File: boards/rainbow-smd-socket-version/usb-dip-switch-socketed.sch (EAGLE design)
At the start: 19 parts, among them SW1 KMR211NGLFS, SW2 110-47-316-41-105000, U1 PIC16F1459-I/SS, U2 PRTR5V0U2X

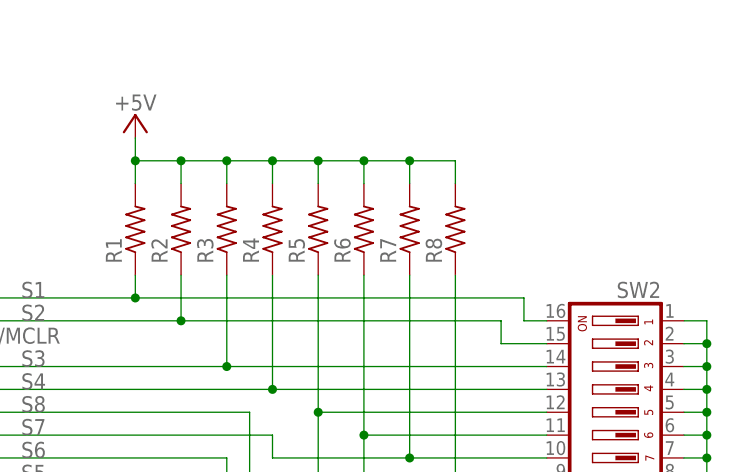
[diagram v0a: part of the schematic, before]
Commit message: add 100k value for pullup resistors R1-R8
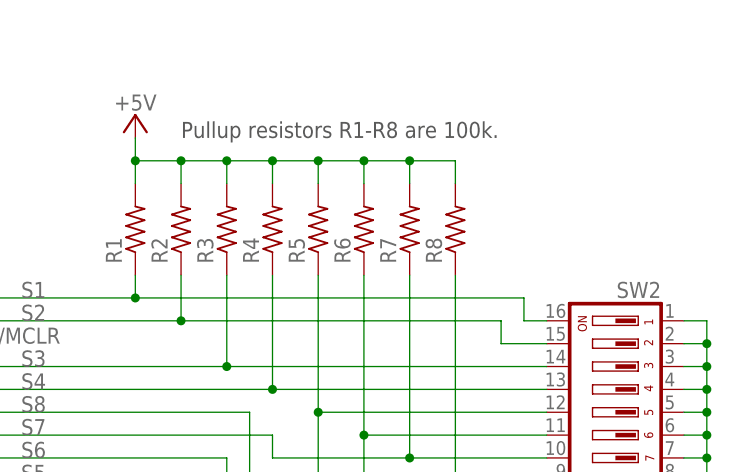
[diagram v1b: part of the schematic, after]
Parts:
- R1, R2, R3, R4, R5, R6, R7, R8: value (none) -> 100k
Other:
- note added: "Pullup resistors R1-R8 are 100k."
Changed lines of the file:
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@@
 <part name="SW2" library="Glen-MillMax-110-47-316-41-105000" deviceset="110-47-316-41-105000" device=""/>
 <part name="SUPPLY7" library="supply2" deviceset="GND" device=""/>
-<part name="R1" library="rcl" deviceset="R-US_" device="R0603"/>
-<part name="R2" library="rcl" deviceset="R-US_" device="R0603"/>
-<part name="R3" library="rcl" deviceset="R-US_" device="R0603"/>
-<part name="R4" library="rcl" deviceset="R-US_" device="R0603"/>
-<part name="R5" library="rcl" deviceset="R-US_" device="R0603"/>
-<part name="R6" library="rcl" deviceset="R-US_" device="R0603"/>
-<part name="R7" library="rcl" deviceset="R-US_" device="R0603"/>
-<part name="R8" library="rcl" deviceset="R-US_" device="R0603"/>
+<part name="R1" library="rcl" deviceset="R-US_" device="R0603" value="100k"/>
+<part name="R2" library="rcl" deviceset="R-US_" device="R0603" value="100k"/>
+<part name="R3" library="rcl" deviceset="R-US_" device="R0603" value="100k"/>
+<part name="R4" library="rcl" deviceset="R-US_" device="R0603" value="100k"/>
+<part name="R5" library="rcl" deviceset="R-US_" device="R0603" value="100k"/>
+<part name="R6" library="rcl" deviceset="R-US_" device="R0603" value="100k"/>
+<part name="R7" library="rcl" deviceset="R-US_" device="R0603" value="100k"/>
+<part name="R8" library="rcl" deviceset="R-US_" device="R0603" value="100k"/>
 <part name="P+4" library="supply1" deviceset="+5V" device=""/>
 </parts>
@@
 <text x="165.1" y="86.36" size="3.81" layer="97">ESD Protection</text>
 <text x="215.9" y="114.3" size="1.778" layer="97" align="top-left">ERG SDS-8-014</text>
+<text x="177.8" y="162.56" size="1.778" layer="97">Pullup resistors R1-R8 are 100k.</text>
 </plain>
 <instances>
@@
 <instance part="SW2" gate="G$1" x="226.06" y="137.16" rot="MR270"/>
 <instance part="SUPPLY7" gate="GND" x="236.22" y="119.38" rot="MR0"/>
-<instance part="R1" gate="G$1" x="172.72" y="152.4" rot="R90"/>
-<instance part="R2" gate="G$1" x="177.8" y="152.4" rot="R90"/>
-<instance part="R3" gate="G$1" x="182.88" y="152.4" rot="R90"/>
-<instance part="R4" gate="G$1" x="187.96" y="152.4" rot="R90"/>
-<instance part="R5" gate="G$1" x="193.04" y="152.4" rot="R90"/>
-<instance part="R6" gate="G$1" x="198.12" y="152.4" rot="R90"/>
-<instance part="R7" gate="G$1" x="203.2" y="152.4" rot="R90"/>
-<instance part="R8" gate="G$1" x="208.28" y="152.4" rot="R90"/>
+<instance part="R1" gate="G$1" x="172.72" y="152.4" smashed="yes" rot="R90">
+<attribute name="NAME" x="171.2214" y="148.59" size="1.778" layer="95" rot="R90"/>
+</instance>
+<instance part="R2" gate="G$1" x="177.8" y="152.4" smashed="yes" rot="R90">
+<attribute name="NAME" x="176.3014" y="148.59" size="1.778" layer="95" rot="R90"/>
+</instance>
+<instance part="R3" gate="G$1" x="182.88" y="152.4" smashed="yes" rot="R90">
+<attribute name="NAME" x="181.3814" y="148.59" size="1.778" layer="95" rot="R90"/>
+</instance>
+<instance part="R4" gate="G$1" x="187.96" y="152.4" smashed="yes" rot="R90">
+<attribute name="NAME" x="186.4614" y="148.59" size="1.778" layer="95" rot="R90"/>
+</instance>
+<instance part="R5" gate="G$1" x="193.04" y="152.4" smashed="yes" rot="R90">
+<attribute name="NAME" x="191.5414" y="148.59" size="1.778" layer="95" rot="R90"/>
+</instance>
+<instance part="R6" gate="G$1" x="198.12" y="152.4" smashed="yes" rot="R90">
+<attribute name="NAME" x="196.6214" y="148.59" size="1.778" layer="95" rot="R90"/>
+</instance>
+<instance part="R7" gate="G$1" x="203.2" y="152.4" smashed="yes" rot="R90">
+<attribute name="NAME" x="201.7014" y="148.59" size="1.778" layer="95" rot="R90"/>
+</instance>
+<instance part="R8" gate="G$1" x="208.28" y="152.4" smashed="yes" rot="R90">
+<attribute name="NAME" x="206.7814" y="148.59" size="1.778" layer="95" rot="R90"/>
+</instance>
 <instance part="P+4" gate="1" x="172.72" y="165.1" smashed="yes" rot="MR0">
 <attribute name="VALUE" x="172.72" y="165.608" size="1.778" layer="96" rot="MR0" align="bottom-center"/>
